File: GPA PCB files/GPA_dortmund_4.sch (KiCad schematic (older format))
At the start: 29 parts, among them U102 AAVID_TO220_HEATSINK, U17 OPA549_KV_11TO-220_11, U18 OPA549_KV_11TO-220_11, U19 INA149SOIC8, X7 MINI-FIT-JR-045569-NA2

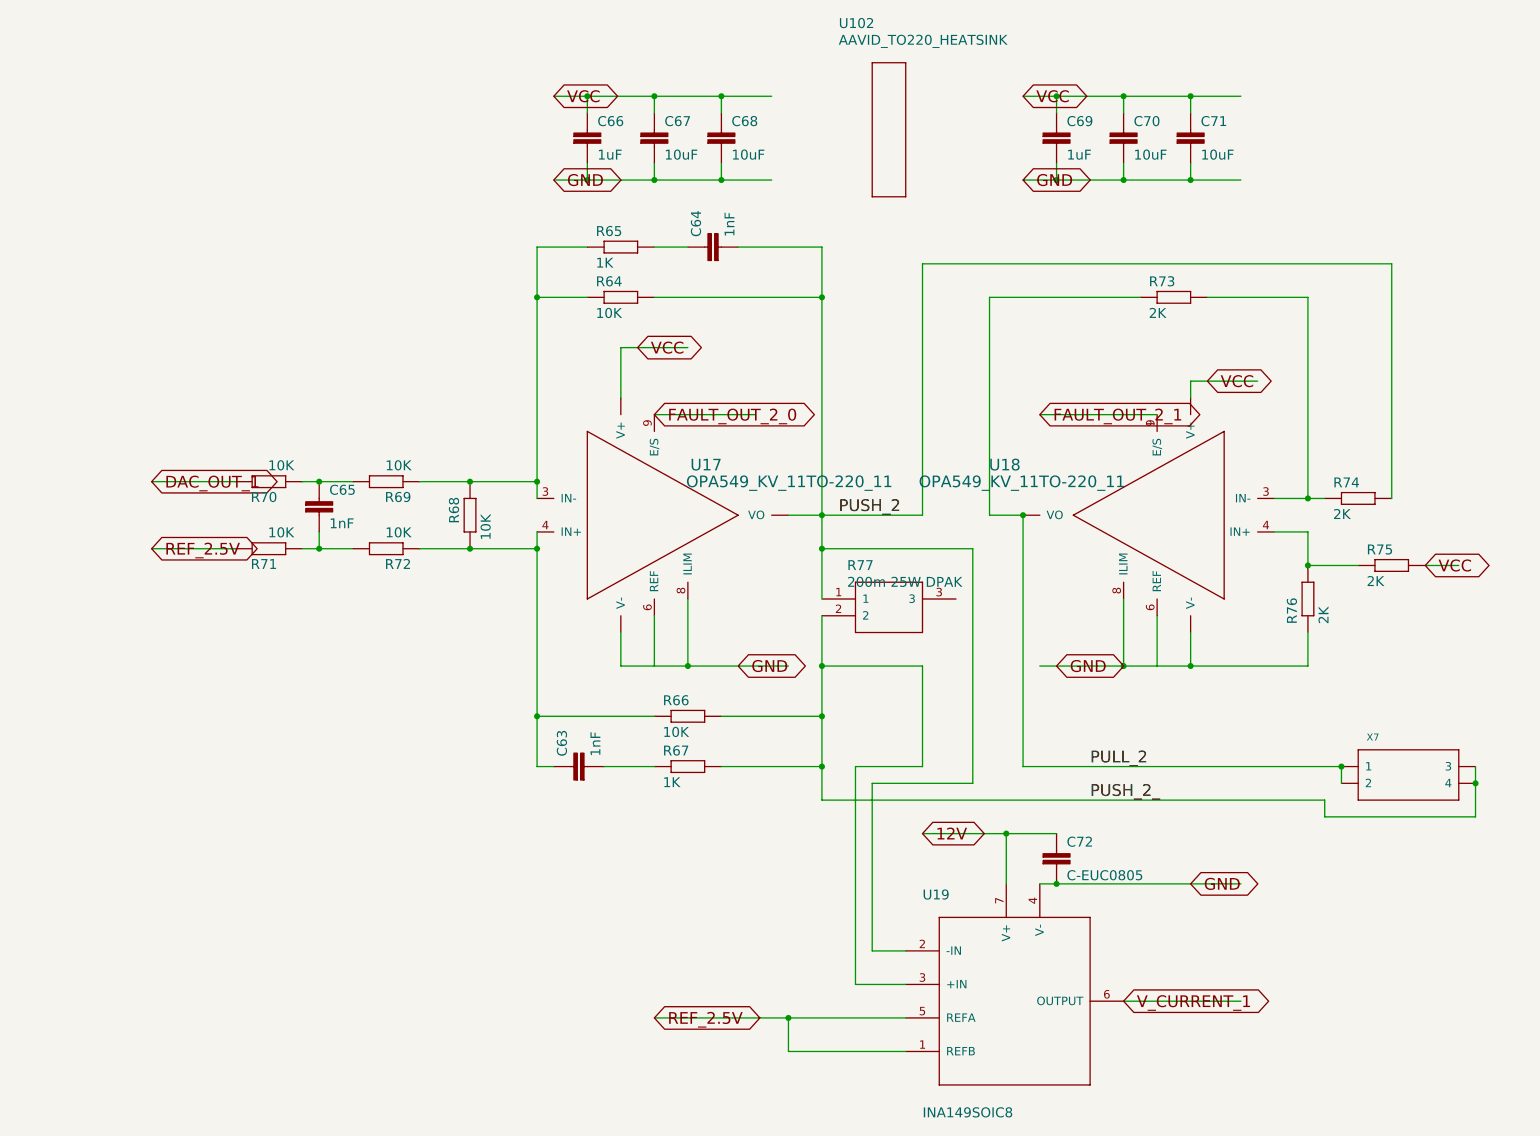
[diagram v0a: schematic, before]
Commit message: fixed schematic after conversion from eagle
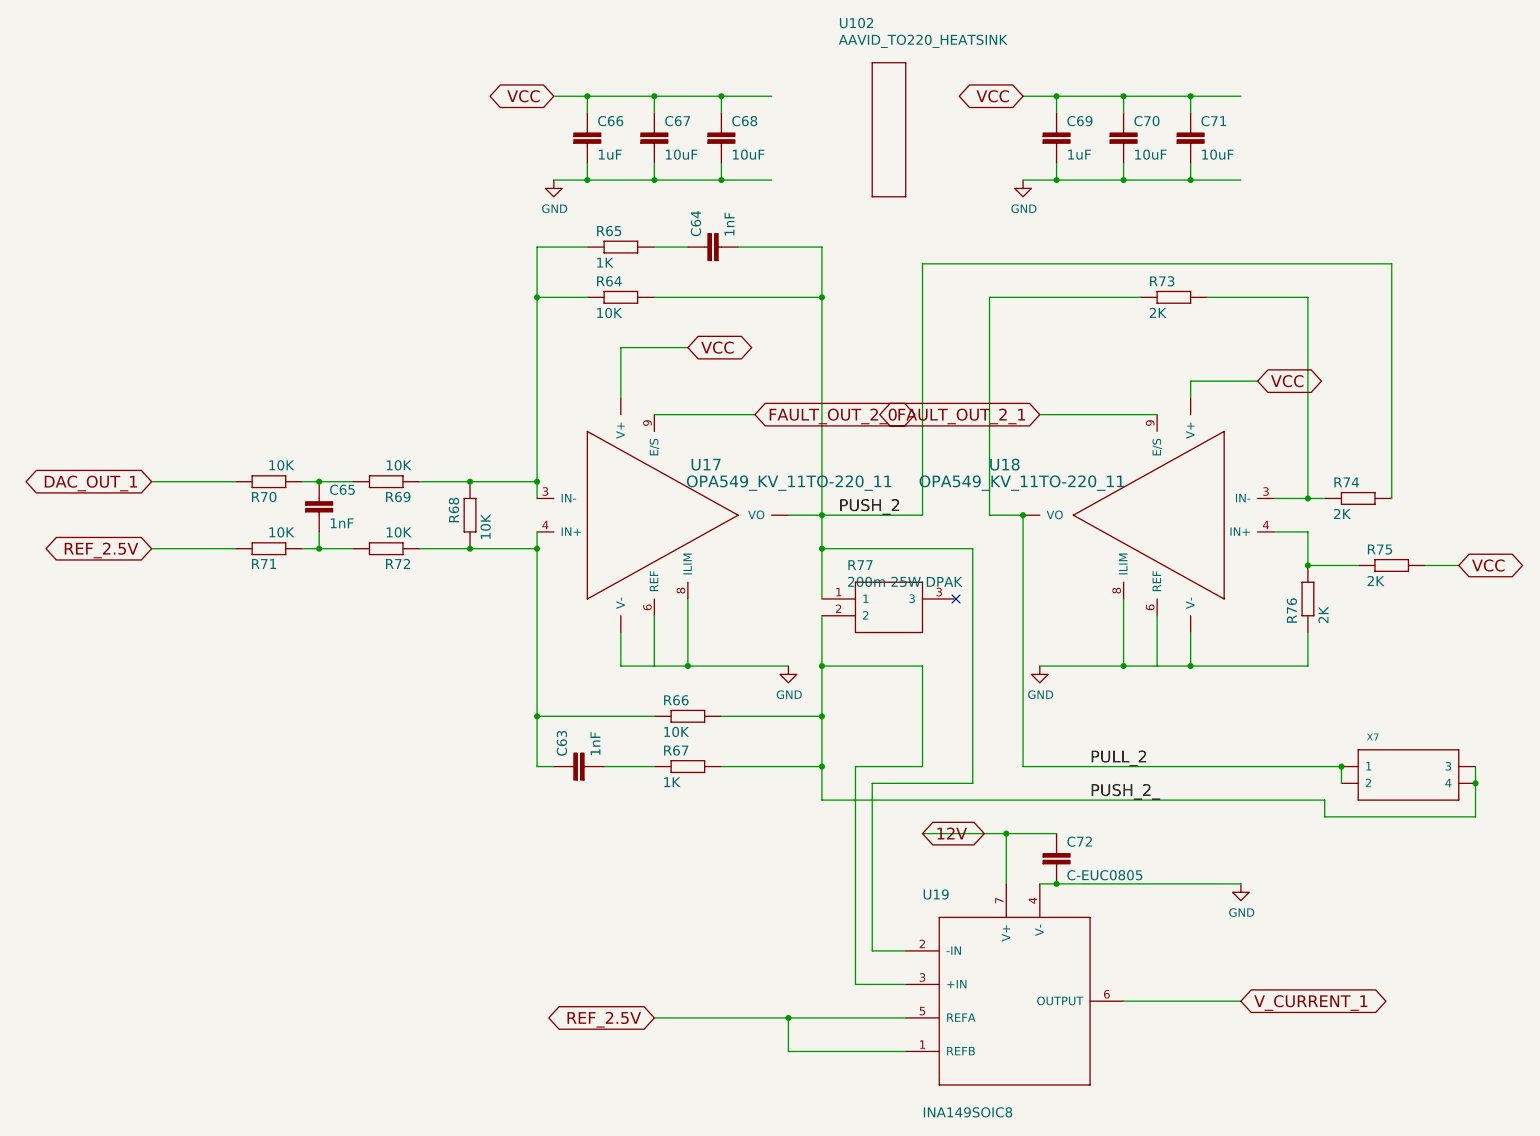
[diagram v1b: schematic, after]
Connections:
- no-connect marks 0 -> 1
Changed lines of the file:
@@
 $Descr A4 11693 8268
 encoding utf-8
-Sheet 1 6
+Sheet 5 6
 Title ""
 Date ""
@@
 Wire Wire Line
 	4600 2800 5000 2800
-Text GLabel 4700 2800 2    70   BiDi ~ 0
+Text GLabel 5000 2800 2    70   BiDi ~ 0
 VCC
 Wire Wire Line
@@
 Wire Wire Line
 	8000 3000 8400 3000
-Text GLabel 8100 3000 2    70   BiDi ~ 0
+Text GLabel 8400 3000 2    70   BiDi ~ 0
 VCC
 Wire Wire Line
 	9400 4100 9600 4100
-Text GLabel 9400 4100 2    70   BiDi ~ 0
+Text GLabel 9600 4100 2    70   BiDi ~ 0
 VCC
 Wire Wire Line
@@
 Connection ~ 4800 1300
 Connection ~ 5200 1300
-Text GLabel 4200 1300 2    70   BiDi ~ 0
+Text GLabel 4200 1300 0    70   BiDi ~ 0
 VCC
 Wire Wire Line
@@
 Connection ~ 7600 1300
 Connection ~ 8000 1300
-Text GLabel 7000 1300 2    70   BiDi ~ 0
+Text GLabel 7000 1300 0    70   BiDi ~ 0
 VCC
 Wire Wire Line
@@
 	5000 4300 5000 4700
 Connection ~ 5000 4700
-Text GLabel 5300 4700 2    70   BiDi ~ 0
-GND
 Wire Wire Line
 	8000 4500 8000 4700
@@
 	8700 4700 8000 4700
 Connection ~ 7600 4700
-Text GLabel 7200 4700 2    70   BiDi ~ 0
-GND
 Connection ~ 8000 4700
 Wire Wire Line
@@
 Connection ~ 4800 1800
 Connection ~ 4400 1800
-Text GLabel 4200 1800 2    70   BiDi ~ 0
-GND
 Wire Wire Line
 	7000 1800 7200 1800
@@
 Connection ~ 7600 1800
 Connection ~ 7200 1800
-Text GLabel 7000 1800 2    70   BiDi ~ 0
-GND
 Wire Wire Line
 	7100 6000 7200 6000
 Wire Wire Line
 	7200 6000 8300 6000
-Text GLabel 8000 6000 2    70   BiDi ~ 0
-GND
 Connection ~ 7200 6000
 Wire Wire Line
@@
 Wire Wire Line
 	2300 4000 1800 4000
-Text GLabel 1800 4000 2    70   BiDi ~ 0
+Text GLabel 1800 4000 0    70   BiDi ~ 0
 REF_2.5V
 Wire Wire Line
@@
 	5600 6800 4800 6800
 Connection ~ 5600 6800
-Text GLabel 4800 6800 2    70   BiDi ~ 0
+Text GLabel 4800 6800 0    70   BiDi ~ 0
 REF_2.5V
 Wire Wire Line
@@
 Wire Wire Line
 	7800 3200 7100 3200
-Text GLabel 7100 3200 2    70   BiDi ~ 0
+Text GLabel 7100 3200 0    70   BiDi ~ 0
 FAULT_OUT_2_1
 Wire Wire Line
 	4800 3200 5400 3200
-Text GLabel 4800 3200 2    70   BiDi ~ 0
+Text GLabel 5400 3200 2    70   BiDi ~ 0
 FAULT_OUT_2_0
 Wire Wire Line
 	2300 3600 1800 3600
-Text GLabel 1800 3600 2    70   BiDi ~ 0
+Text GLabel 1800 3600 0    70   BiDi ~ 0
 DAC_OUT_1
 Wire Wire Line
 	7600 6700 8300 6700
-Text GLabel 7600 6700 2    70   BiDi ~ 0
+Text GLabel 8300 6700 2    70   BiDi ~ 0
 V_CURRENT_1
 $Comp
@@
 	1    0    0    -1
 $EndComp
+$Comp
+L power:GND #PWR?
+U 1 1 61D7A99B
+P 4200 1800
+AR Path="/61ABA20B/61D7A99B" Ref="#PWR?"  Part="1"
+AR Path="/61ABA057/61D7A99B" Ref="#PWR0134"  Part="1"
+F 0 "#PWR0134" H 4200 1550 50  0001 C CNN
+F 1 "GND" H 4205 1627 50  0000 C CNN
+F 2 "" H 4200 1800 50  0001 C CNN
+F 3 "" H 4200 1800 50  0001 C CNN
+	1    4200 1800
+	1    0    0    -1
+$EndComp
+$Comp
+L power:GND #PWR?
+U 1 1 61D7F71B
+P 7000 1800
+AR Path="/61ABA20B/61D7F71B" Ref="#PWR?"  Part="1"
+AR Path="/61ABA057/61D7F71B" Ref="#PWR0135"  Part="1"
+F 0 "#PWR0135" H 7000 1550 50  0001 C CNN
+F 1 "GND" H 7005 1627 50  0000 C CNN
+F 2 "" H 7000 1800 50  0001 C CNN
+F 3 "" H 7000 1800 50  0001 C CNN
+	1    7000 1800
+	1    0    0    -1
+$EndComp
+$Comp
+L power:GND #PWR?
+U 1 1 61D890EB
+P 8300 6000
+AR Path="/61ABA20B/61D890EB" Ref="#PWR?"  Part="1"
+AR Path="/61ABA057/61D890EB" Ref="#PWR0136"  Part="1"
+F 0 "#PWR0136" H 8300 5750 50  0001 C CNN
+F 1 "GND" H 8305 5827 50  0000 C CNN
+F 2 "" H 8300 6000 50  0001 C CNN
+F 3 "" H 8300 6000 50  0001 C CNN
+	1    8300 6000
+	1    0    0    -1
+$EndComp
+$Comp
+L power:GND #PWR?
+U 1 1 61D97556
+P 5600 4700
+AR Path="/61ABA20B/61D97556" Ref="#PWR?"  Part="1"
+AR Path="/61ABA057/61D97556" Ref="#PWR0137"  Part="1"
+F 0 "#PWR0137" H 5600 4450 50  0001 C CNN
+F 1 "GND" H 5605 4527 50  0000 C CNN
+F 2 "" H 5600 4700 50  0001 C CNN
+F 3 "" H 5600 4700 50  0001 C CNN
+	1    5600 4700
+	1    0    0    -1
+$EndComp
+$Comp
+L power:GND #PWR?
+U 1 1 61D9C3BE
+P 7100 4700
+AR Path="/61ABA20B/61D9C3BE" Ref="#PWR?"  Part="1"
+AR Path="/61ABA057/61D9C3BE" Ref="#PWR0138"  Part="1"
+F 0 "#PWR0138" H 7100 4450 50  0001 C CNN
+F 1 "GND" H 7105 4527 50  0000 C CNN
+F 2 "" H 7100 4700 50  0001 C CNN
+F 3 "" H 7100 4700 50  0001 C CNN
+	1    7100 4700
+	1    0    0    -1
+$EndComp
+NoConn ~ 6600 4300
 $EndSCHEMATC

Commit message: more schematic fixes, only 1 ERC warning left (but thats ok)
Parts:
- U17, U18: value OPA549_KV_11TO-220_11 -> OPA549; symbol GPA_dortmund-eagle-import:OPA549_KV_11TO-220_11 -> GPA_dortmund-rescue:OPA549_KV_11TO-220_11-GPA_dortmund-eagle-import
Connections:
- net labels added: +12V
- net labels removed: 12V
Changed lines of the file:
@@
 Text GLabel 5000 2800 2    70   BiDi ~ 0
 VCC
-Wire Wire Line
-	8000 3100 8000 3000
-Wire Wire Line
-	8000 3000 8400 3000
 Text GLabel 8400 3000 2    70   BiDi ~ 0
 VCC
@@
 Wire Wire Line
 	7200 5700 6900 5700
-Text GLabel 6400 5700 2    70   BiDi ~ 0
-12V
 Connection ~ 6900 5700
 Wire Wire Line
-	7800 3200 7100 3200
-Text GLabel 7100 3200 0    70   BiDi ~ 0
+	7800 3200 7700 3200
+Text GLabel 7700 3200 0    70   BiDi ~ 0
 FAULT_OUT_2_1
 Wire Wire Line
-	4800 3200 5400 3200
-Text GLabel 5400 3200 2    70   BiDi ~ 0
+	4800 3200 4850 3200
+Text GLabel 4850 3200 2    70   BiDi ~ 0
 FAULT_OUT_2_0
 Wire Wire Line
@@
 V_CURRENT_1
 $Comp
-L GPA_dortmund-eagle-import:OPA549_KV_11TO-220_11 U17
+L GPA_dortmund-rescue:OPA549_KV_11TO-220_11-GPA_dortmund-eagle-import U17
 U 1 1 3DB02967
 P 4700 3800
 AR Path="/3DB02967" Ref="U17"  Part="1"
 AR Path="/61ABA057/3DB02967" Ref="U17"  Part="1"
-F 0 "U17" H 5014 4059 69  0000 L BNN
-F 1 "OPA549_KV_11TO-220_11" H 4989 3959 69  0000 L BNN
+F 0 "U17" H 4500 3900 69  0000 L BNN
+F 1 "OPA549" H 4500 3800 69  0000 L BNN
 F 2 "GPA_dortmund:TA11B" H 4700 3800 50  0001 C CNN
 F 3 "" H 4700 3800 50  0001 C CNN
@@
 $EndComp
 $Comp
-L GPA_dortmund-eagle-import:OPA549_KV_11TO-220_11 U18
+L GPA_dortmund-rescue:OPA549_KV_11TO-220_11-GPA_dortmund-eagle-import U18
 U 1 1 84ABBA4D
 P 7900 3800
 AR Path="/84ABBA4D" Ref="U18"  Part="1"
 AR Path="/61ABA057/84ABBA4D" Ref="U18"  Part="1"
-F 0 "U18" H 8814 4059 69  0000 L BNN
-F 1 "OPA549_KV_11TO-220_11" H 8189 3959 69  0000 L BNN
+F 0 "U18" H 7900 3900 69  0000 L BNN
+F 1 "OPA549" H 7700 3800 69  0000 L BNN
 F 2 "GPA_dortmund:TA11B" H 7900 3800 50  0001 C CNN
 F 3 "" H 7900 3800 50  0001 C CNN
@@
 $EndComp
 NoConn ~ 6600 4300
+Wire Wire Line
+	8000 3000 8000 3100
+Wire Wire Line
+	8000 3000 8400 3000
+$Comp
+L power:+12V #PWR0147
+U 1 1 61C851E4
+P 6400 5700
+F 0 "#PWR0147" H 6400 5550 50  0001 C CNN
+F 1 "+12V" H 6415 5873 50  0000 C CNN
+F 2 "" H 6400 5700 50  0001 C CNN
+F 3 "" H 6400 5700 50  0001 C CNN
+	1    6400 5700
+	1    0    0    -1
+$EndComp
 $EndSCHEMATC
